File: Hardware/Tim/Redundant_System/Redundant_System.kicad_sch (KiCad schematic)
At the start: 30 parts, among them J1 SOICbite, Q1 IRLML0060TRPBF, U1 RP2040, U2 W25Q64JVZP, Y1 445I23D12M00000

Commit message: Reduntant board has all the stuff?
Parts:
- added C32, C33: 220nF, Capacitor_SMD:C_0603_1608Metric_Pad1.08x0.95mm_HandSolder, symbol Device:C_Small
- added C34: 4.7uF, Capacitor_SMD:C_0603_1608Metric_Pad1.08x0.95mm_HandSolder, symbol Device:C_Small
- added C38: 22nF, Capacitor_SMD:C_0603_1608Metric_Pad1.08x0.95mm_HandSolder, symbol Device:C_Small
- added C39, C40: 22uF, Capacitor_SMD:C_0603_1608Metric_Pad1.08x0.95mm_HandSolder, symbol Device:C_Small
- added C41: 680p, Capacitor_SMD:C_0603_1608Metric_Pad1.08x0.95mm_HandSolder, symbol Device:C_Small
- added C42: 10uF, Capacitor_SMD:C_0603_1608Metric_Pad1.08x0.95mm_HandSolder, symbol Device:C_Small
- added J4: Nichrome, Connector_PinHeader_2.54mm:PinHeader_1x02_P2.54mm_Vertical, symbol Connector:Conn_01x02_Socket
- added JP1, JP2: SolderJumper_2_Open, Jumper:SolderJumper-2_P1.3mm_Open_TrianglePad1.0x1.5mm, symbol Jumper:SolderJumper_2_Open
- added L2: 3.3uH, Terminator_Lib:L_Bourns_SRP1265A, symbol Device:L
- added R23: 81.1k, Resistor_SMD:R_0603_1608Metric_Pad0.98x0.95mm_HandSolder, symbol Device:R_Small
- added R24: 75k, Resistor_SMD:R_0603_1608Metric_Pad0.98x0.95mm_HandSolder, symbol Device:R_Small
- added R25: 5m, Resistor_SMD:R_0603_1608Metric_Pad0.98x0.95mm_HandSolder, symbol Device:R_Small
- added R26, R27: 154k, Resistor_SMD:R_0603_1608Metric_Pad0.98x0.95mm_HandSolder, symbol Device:R_Small
- added R28: 56.2k, Resistor_SMD:R_0603_1608Metric_Pad0.98x0.95mm_HandSolder, symbol Device:R_Small
- added U1: LT3120JV-PBF, Terminator_Lib:LQFN28_Rev0_ADI-M, symbol Terminator_Lib:LT3120JV-PBF
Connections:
- net +3V3: now also JP2.1 (A)
- net GND: now also C34.2, C39.2, C40.2, C41.2, C42.2, J4.2 (Pin_2), R23.2, R24.2, R27.2, U1.11 (GND), U1.18 (GND), U1.22 (GND), U1.29 (PGND), U1.3 (GND)
- net Ch.2A: now reaches U1.5 (GPIO3)
- net Ch.2B: now reaches U1.6 (GPIO4)
- net CUT: now reaches U1.8 (GPIO6)
- net CUT: now also U1.16 (EN/UVLO)
- net Ch.A renamed Ch.1A
- net Ch.B renamed Ch.1B
- new net: C38.2, C39.1, C40.1, J4.1 (Pin_1), R26.1, U1.2 (PVOUT), U1.4 (PVOUT)
- new net: R24.1, U1.14 (RT)
- new net: JP1.2 (B), JP2.2 (B), U1.17 (VIN)
- new net: C41.1, R28.2
- new net: C34.1, U1.12 (MPCC), U1.13 (VCC)
- new net: C42.1, R25.2, U1.15 (SYNC/MODE), U1.19 (PVIN), U1.20 (PVIN), U1.21 (PVIN), U1.6 (ISN)
- new net: C32.1, U1.23 (BST1)
- new net: C32.2, L2.1, U1.24 (SW1), U1.25 (SW1)
- new net: R26.2, R27.1, U1.9 (FB)
- new net: R28.1, U1.10 (VC)
- new net: C33.1, U1.28 (BST2)
- new net: C33.2, L2.2, U1.26 (SW2), U1.27 (SW2)
- new net: C38.1, U1.1 (BST3)
- new net: R23.1, U1.8 (PROG)
- new net +BATT: JP1.1 (A), R25.1, U1.5 (ISP)
- no-connect marks 30 -> 28
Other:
- note added: "Cutdown Circuit"
- note added: "Dan mentioned circuitry to convert to step and direction for encoders"
- note added: "Was this circuit ever tested?"

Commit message: Added color sensors disconnected GPIO in muxing crisis
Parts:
- added D1: USBLC6-2SC6, PCM_Package_TO_SOT_SMD_AKL:SOT-23-6, symbol Diode_TVS_AKL:USBLC6-2SC6
- added J2: USB_C_Receptacle_USB2.0, Connector_USB:USB_C_Receptacle_GCT_USB4105-xx-A_16P_TopMnt_Horizontal, symbol Connector:USB_C_Receptacle_USB2.0
- added R3, R4: 5.1k, Resistor_SMD:R_0402_1005Metric, symbol Device:R_Small
- added TP1, TP2: TestPoint, TestPoint:TestPoint_Pad_D1.0mm, symbol Connector:TestPoint
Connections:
- net GND: now also D1.2 (VN), J2.A1 (GND), J2.A12 (GND), J2.B1 (GND), J2.B12 (GND), J2.S1 (SHIELD), R3.2, R4.2, TP1.1
- net USB_D+ renamed R_USB_D+
- net R_USB_D+: now also D1.1 (L1)
- net USB_D- renamed R_USB_D-
- net R_USB_D-: now also D1.3 (L2)
- new net: J2.A5 (CC1), R3.1
- new net: D1.6 (L1), J2.A6 (D+), J2.B6 (D+)
- new net: D1.4 (L2), J2.A7 (D-), J2.B7 (D-)
- new net: J2.B5 (CC2), R4.1
- new net VBUS: D1.5 (VP), J2.A4 (VBUS), J2.A9 (VBUS), J2.B4 (VBUS), J2.B9 (VBUS), TP2.1
- no-connect marks 28 -> 30
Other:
- note added: "Power"
- note added: "Redundant USB"
- note added: "Transient Voltage Suppression"

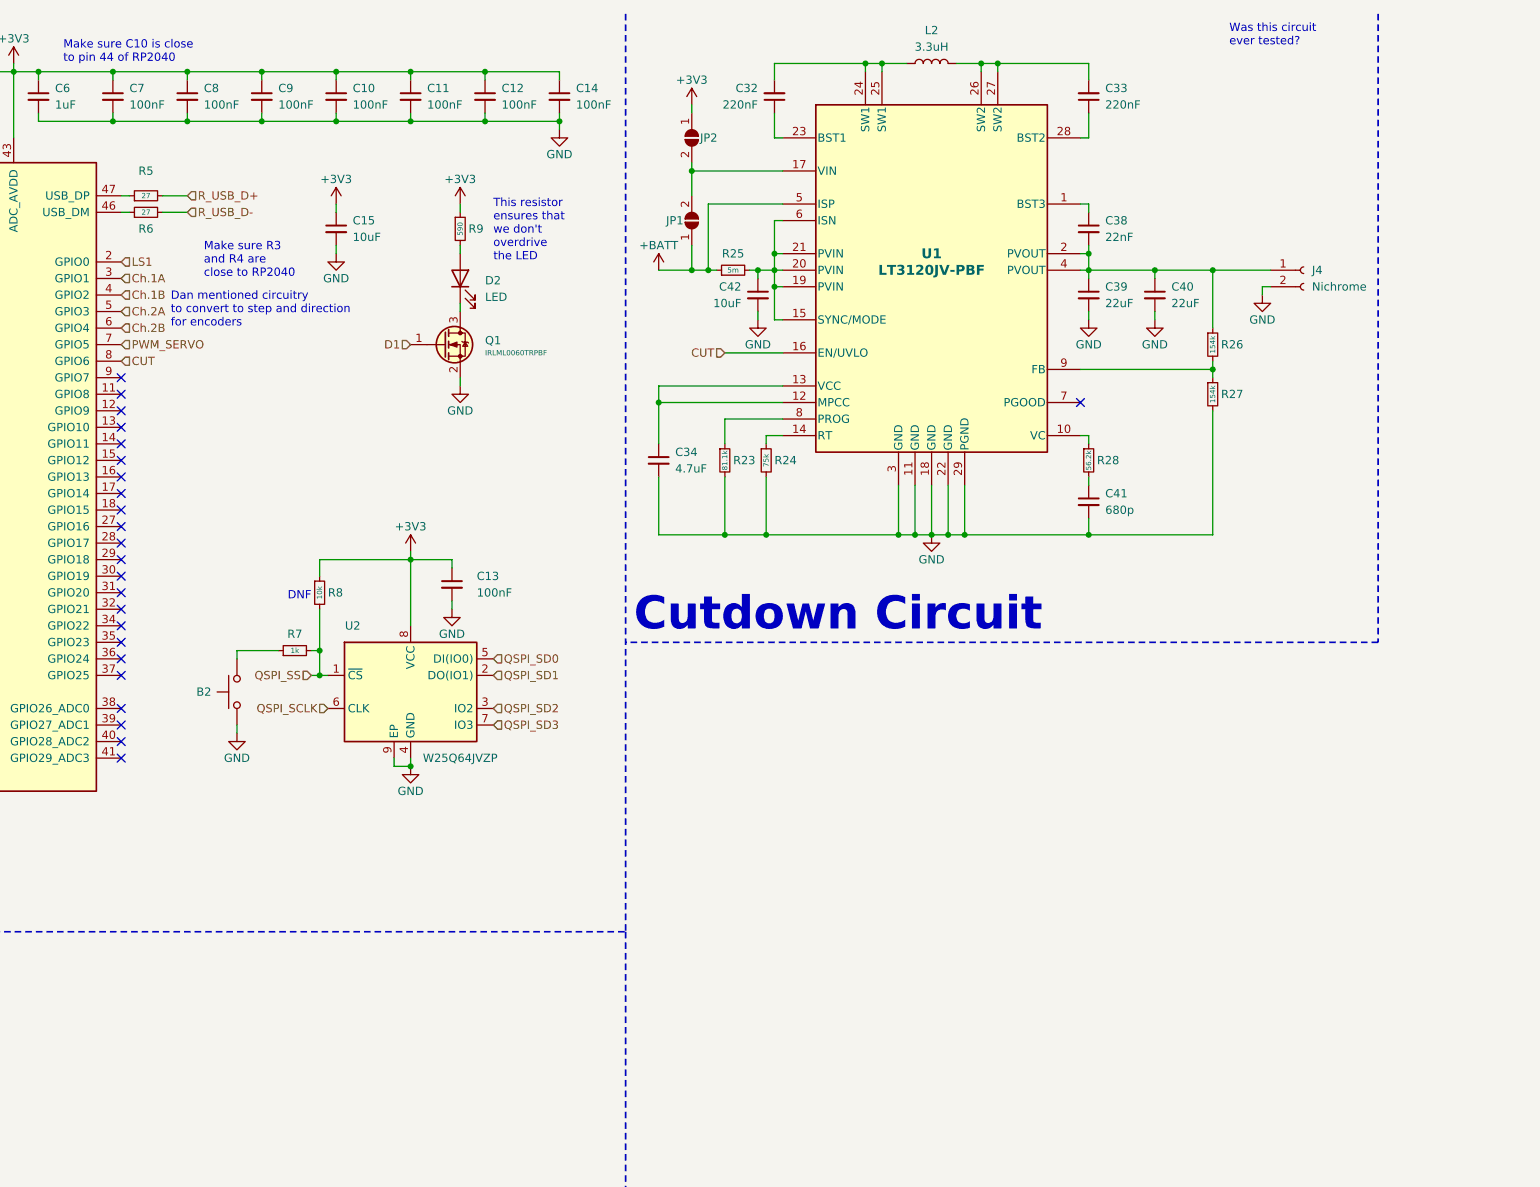
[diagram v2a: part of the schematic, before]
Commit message: Made it all one board due to large space allowed
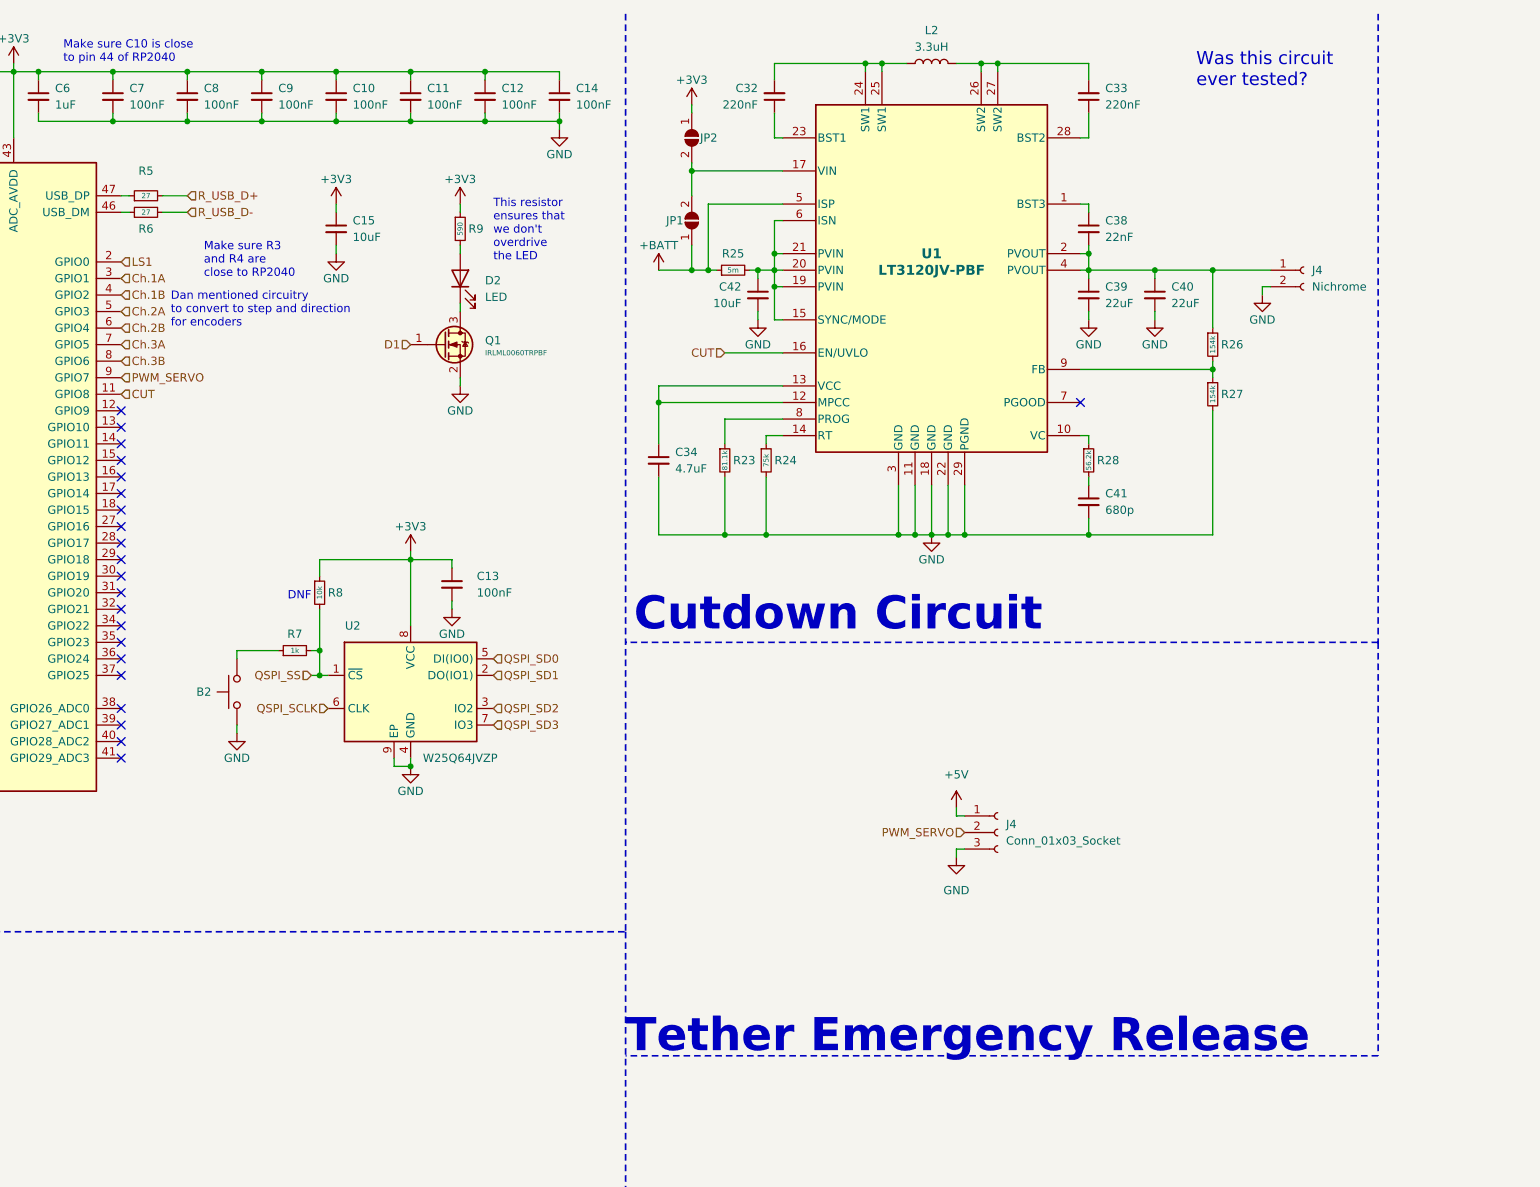
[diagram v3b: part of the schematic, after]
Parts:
- added J4: Conn_01x03_Socket, symbol Connector:Conn_01x03_Socket
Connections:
- net CUT: now also U1.11 (GPIO8); no longer U1.8 (GPIO6)
- net GND: now also J4.3 (Pin_3)
- net PWM_SERVO: now also U1.9 (GPIO7), J4.2 (Pin_2); no longer U1.7 (GPIO5)
- new net +5V: J4.1 (Pin_1)
- new net Ch.3A: U1.7 (GPIO5)
- new net Ch.3B: U1.8 (GPIO6)
- no-connect marks 30 -> 28
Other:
- note added: "Tether Emergency Release"
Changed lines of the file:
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@@
   (no_connect (at 116.84 109.22))
   (no_connect (at 369.57 50.8))
-  (no_connect (at 116.84 68.58))
   (no_connect (at 20.32 129.54))
   (no_connect (at 116.84 104.14))
-  (no_connect (at 116.84 71.12))
   (no_connect (at 116.84 93.98))
   (no_connect (at 116.84 124.46))
@@
     (stroke (width 0) (type default))
   )
+  (wire (pts (xy 245.11 140.97) (xy 246.38 140.97))
+    (stroke (width 0) (type default))
+  )
   (wire (pts (xy 134.62 110.49) (xy 140.97 110.49))
     (stroke (width 0) (type default))
@@
     (stroke (width 0) (type default))
   )
+  (polyline (pts (xy 309.88 109.22) (xy 309.88 172.72))
+    (stroke (width 0.254) (type dash))
+  )
   (wire (pts (xy 236.22 85.09) (xy 236.22 92.71))
     (stroke (width 0) (type default))
@@
     (stroke (width 0) (type default))
   )
+  (polyline (pts (xy 309.88 172.72) (xy 194.31 172.72))
+    (stroke (width 0.254) (type dash))
+  )
+  (wire (pts (xy 245.11 134.62) (xy 245.11 135.89))
+    (stroke (width 0) (type default))
+  )
   (wire (pts (xy 369.57 40.64) (xy 370.84 40.64))
     (stroke (width 0) (type default))
@@
     (stroke (width 0.254) (type dash))
   )
+  (wire (pts (xy 245.11 142.24) (xy 245.11 140.97))
+    (stroke (width 0) (type default))
+  )
   (wire (pts (xy 100.33 21.59) (xy 104.14 21.59))
     (stroke (width 0) (type default))
@@
     (stroke (width 0) (type default))
   )
+  (wire (pts (xy 245.11 135.89) (xy 246.38 135.89))
+    (stroke (width 0) (type default))
+  )
   (polyline (pts (xy 194.31 153.67) (xy 194.31 284.48))
     (stroke (width 0.254) (type dash))
@@
     (effects (font (size 1.27 1.27)) (justify left bottom))
   )
-  (text "Was this circuit\never tested?" (at 287.02 17.78 0)
-    (effects (font (size 1.27 1.27) (color 255 0 0 1)) (justify left bottom))
+  (text "Was this circuit\never tested?" (at 281.94 24.13 0)
+    (effects (font (size 2 2) (color 255 0 0 1)) (justify left bottom))
   )
   (text "Dan mentioned circuitry\nto convert to step and direction\nfor encoders"
@@
     (effects (font (size 1.27 1.27)) (justify left bottom))
   )
+  (text "Tether Emergency Release" (at 194.31 172.72 0)
+    (effects (font (size 5.08 5.08) (thickness 1.016) bold) (justify left bottom))
+  )
   (text "Redundant USB" (at 337.82 73.66 0)
     (effects (font (size 2.54 2.54) (thickness 0.508) bold) (justify left bottom))
@@
     (effects (font (size 1.27 1.27)) (justify right))
   )
-  (hierarchical_label "CUT" (shape input) (at 116.84 66.04 0) (fields_autoplaced)
+  (hierarchical_label "CUT" (shape input) (at 116.84 71.12 0) (fields_autoplaced)
     (effects (font (size 1.27 1.27)) (justify left))
   )
@@
     (effects (font (size 1.27 1.27)) (justify left))
   )
+  (hierarchical_label "Ch.3A" (shape input) (at 116.84 63.5 0) (fields_autoplaced)
+    (effects (font (size 1.27 1.27)) (justify left))
+  )
   (hierarchical_label "Ch.2A" (shape input) (at 116.84 58.42 0) (fields_autoplaced)
     (effects (font (size 1.27 1.27)) (justify left))
@@
     (effects (font (size 1.27 1.27)) (justify left))
   )
+  (hierarchical_label "PWM_SERVO" (shape input) (at 246.38 138.43 180) (fields_autoplaced)
+    (effects (font (size 1.27 1.27)) (justify right))
+  )
   (hierarchical_label "QSPI_SS" (shape input) (at 146.05 114.3 180) (fields_autoplaced)
     (effects (font (size 1.27 1.27)) (justify right))
   )
+  (hierarchical_label "Ch.3B" (shape input) (at 116.84 66.04 0) (fields_autoplaced)
+    (effects (font (size 1.27 1.27)) (justify left))
+  )
   (hierarchical_label "D1" (shape input) (at 161.29 63.5 180) (fields_autoplaced)
     (effects (font (size 1.27 1.27)) (justify right))
   )
-  (hierarchical_label "PWM_SERVO" (shape input) (at 116.84 63.5 0) (fields_autoplaced)
+  (hierarchical_label "PWM_SERVO" (shape input) (at 116.84 68.58 0) (fields_autoplaced)
     (effects (font (size 1.27 1.27)) (justify left))
   )
@@
     )
   )
+  (symbol (lib_name "GND_1") (lib_id "power:GND") (at 245.11 142.24 0) (unit 1)
+    (in_bom yes) (on_board yes) (dnp no) (fields_autoplaced)
+    (property "Reference" "#PWR031" (at 245.11 148.59 0)
+      (effects (font (size 1.27 1.27)) hide)
+    )
+    (property "Value" "GND" (at 245.11 147.32 0)
+      (effects (font (size 1.27 1.27)))
+    )
+    (property "Footprint" "" (at 245.11 142.24 0)
+      (effects (font (size 1.27 1.27)) hide)
+    )
+    (property "Datasheet" "" (at 245.11 142.24 0)
+      (effects (font (size 1.27 1.27)) hide)
+    )
+    (pin "1")
+    (instances
+      (project "Redundant_System"
+        (path "/26e62c7f-f27c-4940-85ae-9c569ff0337a"
+          (reference "#PWR031") (unit 1)
+        )
+      )
+    )
+  )
   (symbol (lib_id "Device:LED") (at 168.91 53.34 90) (unit 1)
     (in_bom yes) (on_board yes) (dnp no) (fields_autoplaced)
@@
     )
   )
+  (symbol (lib_id "Connector:Conn_01x03_Socket") (at 251.46 138.43 0) (unit 1)
+    (in_bom yes) (on_board yes) (dnp no) (fields_autoplaced)
+    (property "Reference" "J4" (at 252.73 137.16 0)
+      (effects (font (size 1.27 1.27)) (justify left))
+    )
+    (property "Value" "Conn_01x03_Socket" (at 252.73 139.7 0)
+      (effects (font (size 1.27 1.27)) (justify left))
+    )
+    (property "Footprint" "" (at 251.46 138.43 0)
+      (effects (font (size 1.27 1.27)) hide)
+    )
+    (property "Datasheet" "~" (at 251.46 138.43 0)
+      (effects (font (size 1.27 1.27)) hide)
+    )
+    (pin "1")
+    (pin "2")
+    (pin "3")
+    (instances
+      (project "Redundant_System"
+        (path "/26e62c7f-f27c-4940-85ae-9c569ff0337a"
+          (reference "J4") (unit 1)
+        )
+      )
+    )
+  )
   (symbol (lib_id "power:+3V3") (at 100.33 20.32 0) (unit 1)
     (in_bom yes) (on_board yes) (dnp no)
@@
         )
       )
+    )
+  )
+  (symbol (lib_id "power:+5V") (at 245.11 134.62 0) (unit 1)
+    (in_bom yes) (on_board yes) (dnp no) (fields_autoplaced)
+    (property "Reference" "#PWR032" (at 245.11 138.43 0)
+      (effects (font (size 1.27 1.27)) hide)
+    )
+    (property "Value" "+5V" (at 245.11 129.54 0)
+      (effects (font (size 1.27 1.27)))
+    )
+    (property "Footprint" "" (at 245.11 134.62 0)
+      (effects (font (size 1.27 1.27)) hide)
+    )
+    (property "Datasheet" "" (at 245.11 134.62 0)
+      (effects (font (size 1.27 1.27)) hide)
+    )
+    (pin "1")
+    (instances
+      (project "Redundant_System"
+        (path "/26e62c7f-f27c-4940-85ae-9c569ff0337a"
+          (reference "#PWR032") (unit 1)
+        )
+      )
